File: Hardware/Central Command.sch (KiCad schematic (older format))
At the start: 18 parts, among them P101 CONN_01X10, P102 CONN_01X10, P103 CONN_01X04, P104 CONN_01X02, P105 CONN_01X04, P106 CONN_01X02, U101 STM32F030C8, Y101 Crystal

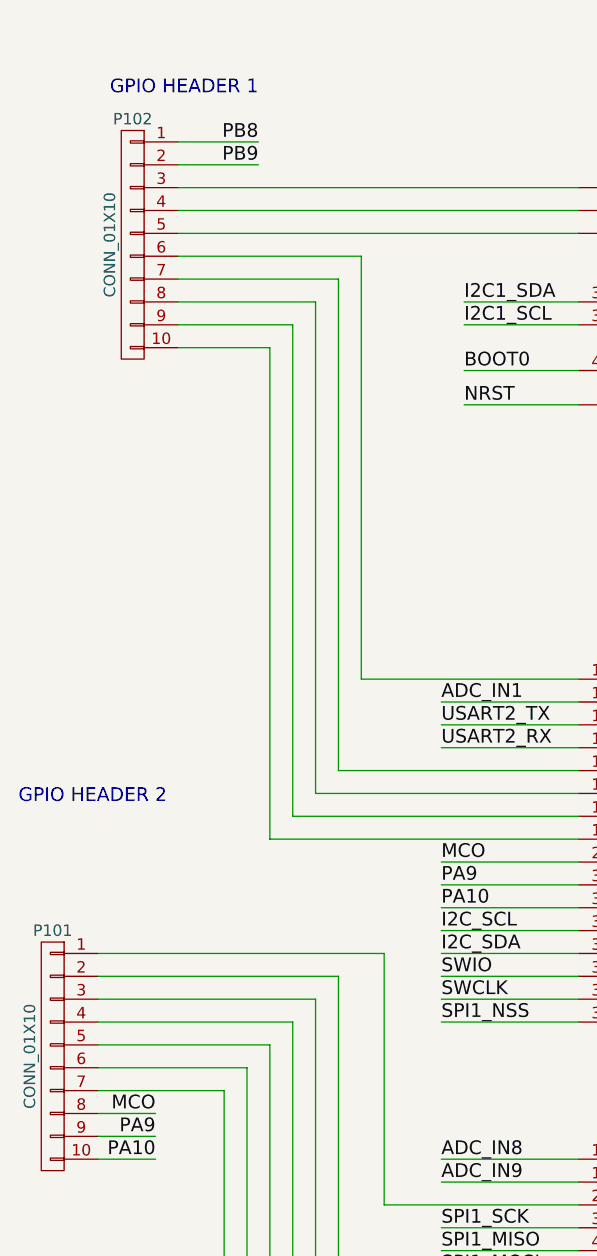
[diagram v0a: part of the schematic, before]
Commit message: - Added Documentation folder - Move cad files to the hardware folder - generated the html BOM
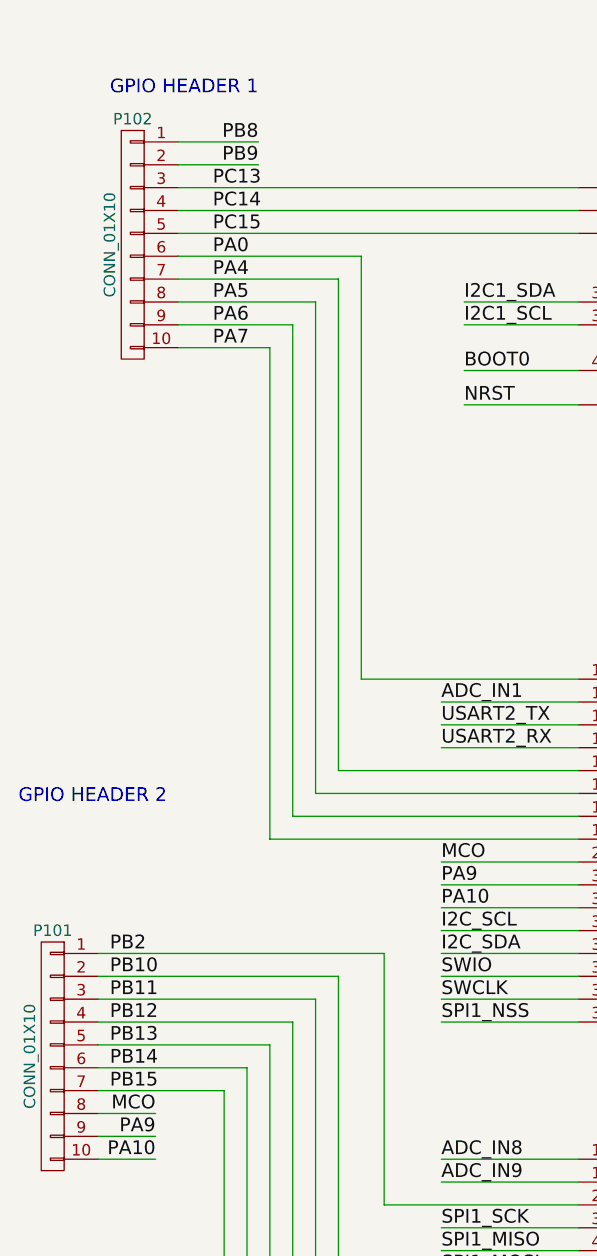
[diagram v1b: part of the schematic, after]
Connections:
- net PA0: now reaches P102.6 (P6), U101.10 (PA0/WKUP1)
- net PA4: now reaches P102.7 (P7), U101.14 (PA4)
- net PA5: now reaches P102.8 (P8), U101.15 (PA5)
- net PA6: now reaches P102.9 (P9), U101.16 (PA6)
- net PA7: now reaches P102.10 (P10), U101.17 (PA7)
- net PB2: now reaches P101.1 (P1), U101.20 (PB2)
- net PB10: now reaches P101.2 (P2), U101.21 (PB10)
- net PB11: now reaches P101.3 (P3), U101.22 (PB11)
- net PB12: now reaches P101.4 (P4), U101.25 (PB12)
- net PB13: now reaches P101.5 (P5), U101.26 (PB13)
- net PB14: now reaches P101.6 (P6), U101.27 (PB14)
- net PB15: now reaches P101.7 (P7), U101.28 (PB15)
- net PC13: now reaches P102.3 (P3), U101.2 (PC13)
- net PC14: now reaches P102.4 (P4), U101.3 (PC14-OSC32_IN)
- net PC15: now reaches P102.5 (P5), U101.4 (PC15-OSC32_OUT)
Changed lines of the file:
@@
 encoding utf-8
 Sheet 1 3
-Title ""
-Date ""
-Rev ""
-Comp ""
-Comment1 ""
-Comment2 ""
-Comment3 ""
-Comment4 ""
+Title "Central Command"
+Date "2016-01-14"
+Rev "0"
+Comp "Contextual Electronics"
+Comment1 "CEDOC-0603"
+Comment2 "contextualelectronics.com"
+Comment3 "N/A"
+Comment4 "N/A"
 $EndDescr
 $Comp
@@
 	9950 700  9950 850
 Connection ~ 9700 700
+Text Label 1650 1600 0    60   ~ 0
+PC13
+Text Label 1650 1700 0    60   ~ 0
+PC14
+Text Label 1650 1800 0    60   ~ 0
+PC15
+Text Label 1650 1900 0    60   ~ 0
+PA0
+Text Label 1650 2000 0    60   ~ 0
+PA4
+Text Label 1650 2100 0    60   ~ 0
+PA5
+Text Label 1650 2200 0    60   ~ 0
+PA6
+Text Label 1650 2300 0    60   ~ 0
+PA7
+Text Label 1200 4950 0    60   ~ 0
+PB2
+Text Label 1200 5050 0    60   ~ 0
+PB10
+Text Label 1200 5150 0    60   ~ 0
+PB11
+Text Label 1200 5250 0    60   ~ 0
+PB12
+Text Label 1200 5350 0    60   ~ 0
+PB13
+Text Label 1200 5450 0    60   ~ 0
+PB14
+Text Label 1200 5550 0    60   ~ 0
+PB15
 $EndSCHEMATC
